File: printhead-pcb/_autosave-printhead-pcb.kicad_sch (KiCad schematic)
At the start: 25 parts, among them J1 Power, J3 DATA, U1 PCA9615DP, U6 AP7361C-33E

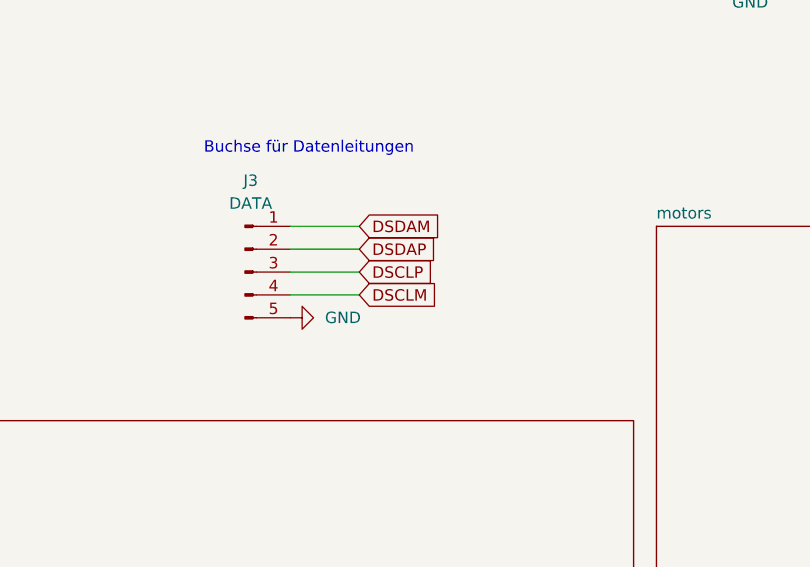
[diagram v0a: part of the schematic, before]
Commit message: version that almost has it but no matter how hard i try i cant seem to make all connections with just one layer, so ill have to use two layers
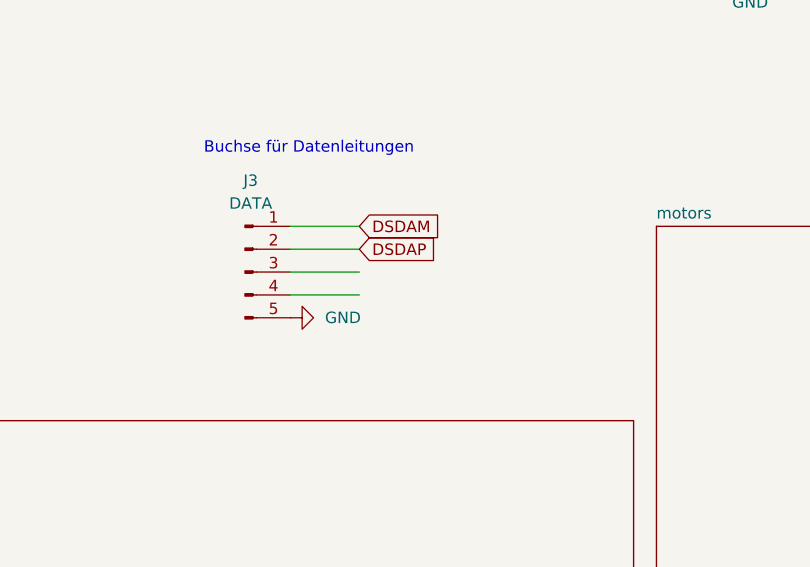
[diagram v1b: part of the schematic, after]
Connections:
- net DSCLM: no longer J3.4 (Pin_4)
- net DSCLP: no longer J3.3 (Pin_3)
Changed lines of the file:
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@@
-		)
-	)
-	(global_label "DSCLP"
-		(shape input)
-		(at 168.91 95.25 0)
-		(fields_autoplaced yes)
-		(effects
-			(font
-				(size 1.27 1.27)
-			)
-			(justify left)
-		)
-		(property "Intersheetrefs" "${INTERSHEET_REFS}"
-			(at 177.9428 95.25 0)
-			(effects
-				(font
-					(size 1.27 1.27)
-				)
-				(justify left)
-				(hide yes)
-			)
 		)
 	)
@@
 			(effects
 				(font
-					(size 1.27 1.27)
-				)
-				(justify left)
-				(hide yes)
-			)
-		)
-	)
-	(global_label "DSCLM"
-		(shape input)
-		(at 168.91 97.79 0)
-		(fields_autoplaced yes)
-		(effects
-			(font
-				(size 1.27 1.27)
-			)
-			(justify left)
-		)
-		(property "Intersheetrefs" "${INTERSHEET_REFS}"
-			(at 178.1242 97.79 0)
-			(effects
-				(font
